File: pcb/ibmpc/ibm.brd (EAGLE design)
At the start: 124 x 56 mm, 32 parts, among them J2 ATX24RH

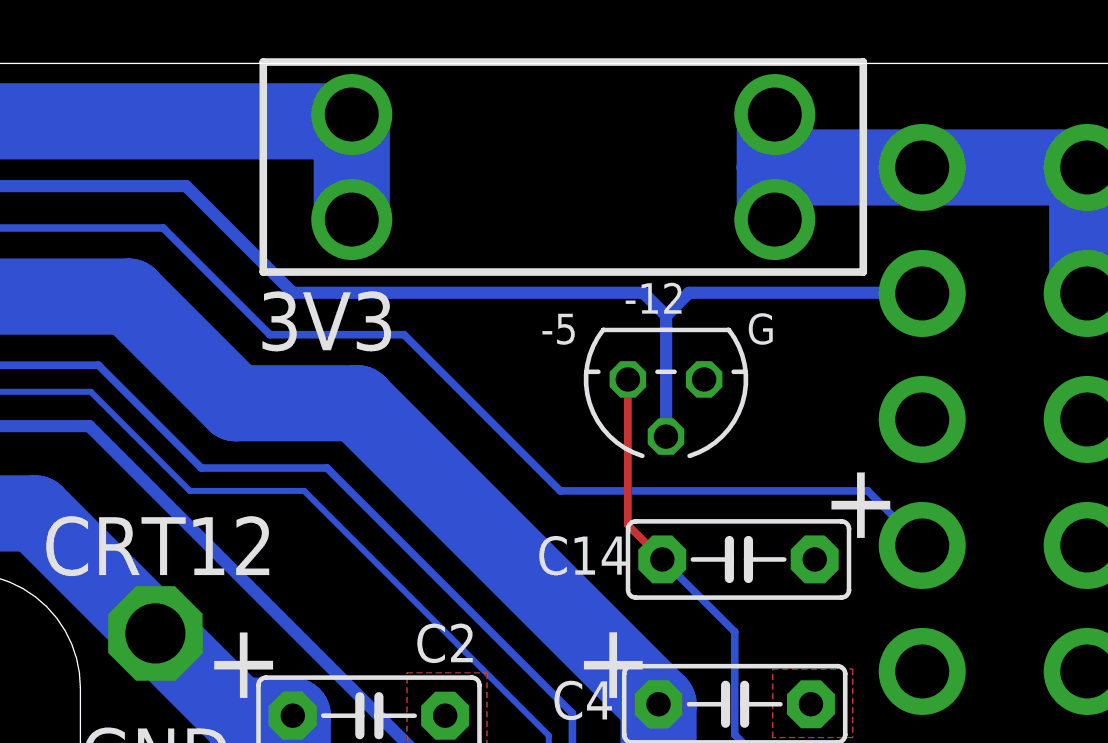
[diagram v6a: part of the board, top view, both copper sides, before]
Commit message: switched back to 7905
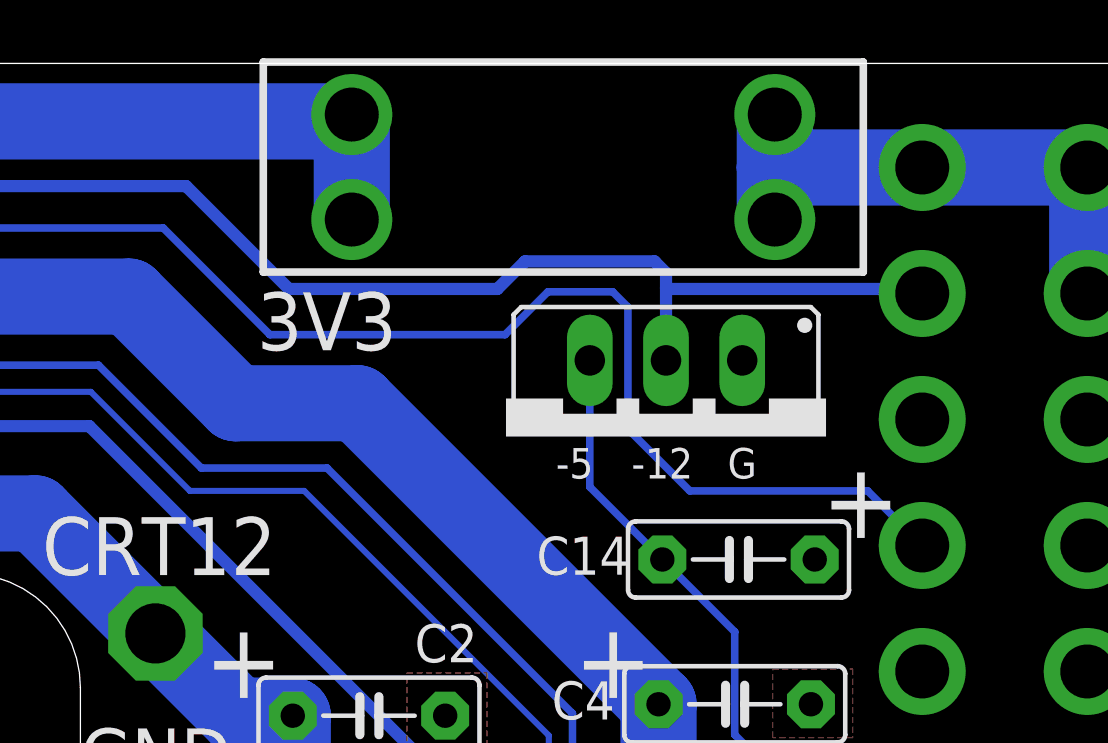
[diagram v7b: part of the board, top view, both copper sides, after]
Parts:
- removed IC2: (no value), linear:TO92
- added IC1: (no value), v-reg:79XXS
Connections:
- net GND: now also IC1.GND; no longer IC2.1
- net N$2: now also IC1.IN; no longer IC2.2
- net N$7: now also IC1.OUT; no longer IC2.3
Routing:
- net N$3: track 98.9 -> 102.5 mm
- net N$2: track 83.3 -> 82.1 mm
- net N$7: track 98.4 -> 99.6 mm
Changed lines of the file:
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@@
 <rectangle x1="67.823" y1="38.576" x2="72.014" y2="43.529" layer="41"/>
 <text x="15.6906" y="18.3234" size="2.54" layer="25" distance="35" align="center">picoRC.com</text>
-<text x="99.695" y="47.149" size="1.016" layer="25" rot="R180" align="center">G</text>
-<text x="96.139" y="48.165" size="1.016" layer="25" rot="R180" align="center">-12</text>
-<text x="92.964" y="47.149" size="1.016" layer="25" rot="R180" align="center">-5</text>
+<text x="99.06" y="42.672" size="1.016" layer="25" rot="R180" align="center">G</text>
+<text x="96.393" y="42.672" size="1.016" layer="25" rot="R180" align="center">-12</text>
+<text x="93.472" y="42.672" size="1.016" layer="25" rot="R180" align="center">-5</text>
 <text x="85.217" y="47.403" size="1.9304" layer="25" rot="R180" align="center">3V3</text>
 <text x="87.122" y="0.921" size="1.6764" layer="25" rot="R180" align="center">12V</text>
@@
 </element>
 <element name="U$7" library="apricot" package="M3_MOUNTING_HOLE_PACK" value="M3_MOUNTING_HOLE" x="80" y="22.75" smashed="yes"/>
-<element name="IC2" library="linear" library_urn="urn:adsk.eagle:library:262" package="TO92" package3d_urn="urn:adsk.eagle:package:16416/2" value="" x="96.52" y="45.466" smashed="yes" rot="R180">
-<attribute name="POPULARITY" value="0" x="96.52" y="45.466" size="1.778" layer="27" rot="R180" display="off"/>
-<attribute name="VALUE" x="93.599" y="46.736" size="1.27" layer="27" ratio="10" rot="R180"/>
+<element name="IC1" library="v-reg" library_urn="urn:adsk.eagle:library:409" package="79XXS" package3d_urn="urn:adsk.eagle:package:30343/1" value="" x="96.52" y="43.561" smashed="yes" rot="R180">
+<attribute name="POPULARITY" value="3" x="96.52" y="42.545" size="1.778" layer="27" rot="R180" display="off"/>
+<attribute name="VALUE" x="101.6" y="51.181" size="1.27" layer="27" ratio="10" rot="R180"/>
 </element>
 </elements>
@@
 <contactref element="U$7" pad="P$1"/>
 <contactref element="U$7" pad="P$2"/>
-<contactref element="IC2" pad="1"/>
 <wire x1="79.5" y1="30" x2="79.5" y2="23.25" width="2.54" layer="16"/>
 <wire x1="79.5" y1="23.25" x2="80" y2="22.75" width="2.54" layer="16"/>
+<contactref element="IC1" pad="GND"/>
 </signal>
 <signal name="+5V">
@@
 <contactref element="J2" pad="14"/>
 <contactref element="U$1" pad="P$12"/>
-<wire x1="105.061" y1="48.332" x2="105.038" y2="48.355" width="0.4064" layer="16"/>
-<wire x1="105.038" y1="48.355" x2="97.287" y2="48.355" width="0.4064" layer="16"/>
-<wire x1="97.287" y1="48.355" x2="96.525" y2="47.593" width="0.4064" layer="16"/>
-<wire x1="96.525" y1="47.593" x2="95.763" y2="48.355" width="0.4064" layer="16"/>
-<wire x1="95.763" y1="48.355" x2="84.079" y2="48.355" width="0.4064" layer="16"/>
+<wire x1="105.061" y1="48.332" x2="104.911" y2="48.482" width="0.4064" layer="16"/>
 <wire x1="40.55" y1="51.911" x2="36.359" y2="47.72" width="0.4064" layer="16"/>
 <wire x1="36.359" y1="47.72" x2="36.359" y2="46.577" width="0.4064" layer="16"/>
@@
 <wire x1="36.359" y1="46.577" x2="36.359" y2="41.059" width="0.4064" layer="1"/>
 <wire x1="36.359" y1="41.059" x2="36.3" y2="41" width="0.4064" layer="1"/>
-<wire x1="84.079" y1="48.355" x2="80.523" y2="51.911" width="0.4064" layer="16"/>
+<wire x1="83.952" y1="48.482" x2="80.523" y2="51.911" width="0.4064" layer="16"/>
 <wire x1="80.523" y1="51.911" x2="40.55" y2="51.911" width="0.4064" layer="16"/>
-<contactref element="IC2" pad="2"/>
-<wire x1="96.525" y1="43.566" x2="96.52" y2="43.561" width="0.4064" layer="16"/>
-<wire x1="96.525" y1="47.593" x2="96.525" y2="43.566" width="0.4064" layer="16"/>
+<contactref element="IC1" pad="IN"/>
+<wire x1="96.52" y1="49.022" x2="96.139" y2="49.403" width="0.4064" layer="16"/>
+<wire x1="96.139" y1="49.403" x2="91.821" y2="49.403" width="0.4064" layer="16"/>
+<wire x1="90.9" y1="48.482" x2="83.952" y2="48.482" width="0.4064" layer="16"/>
+<wire x1="96.52" y1="46.101" x2="96.52" y2="48.514" width="0.4064" layer="16"/>
+<wire x1="96.52" y1="48.514" x2="96.52" y2="49.022" width="0.4064" layer="16"/>
+<wire x1="91.821" y1="49.403" x2="90.9" y2="48.482" width="0.4064" layer="16"/>
+<wire x1="96.552" y1="48.482" x2="96.52" y2="48.514" width="0.4064" layer="16"/>
+<wire x1="104.911" y1="48.482" x2="96.552" y2="48.482" width="0.4064" layer="16"/>
 </signal>
 <signal name="N$3">
@@
 <wire x1="28.39" y1="39.783" x2="24.633" y2="39.783" width="0.2032" layer="1"/>
 <wire x1="29.596" y1="40.989" x2="28.39" y2="39.783" width="0.2032" layer="1"/>
-<wire x1="87.789" y1="46.958" x2="83.317" y2="46.958" width="0.254" layer="16"/>
-<wire x1="103.242" y1="41.751" x2="92.996" y2="41.751" width="0.254" layer="16"/>
-<wire x1="92.996" y1="41.751" x2="87.789" y2="46.958" width="0.254" layer="16"/>
+<wire x1="103.242" y1="41.751" x2="97.314" y2="41.751" width="0.254" layer="16"/>
+<wire x1="95.25" y1="47.879" x2="94.742" y2="48.387" width="0.254" layer="16"/>
+<wire x1="94.742" y1="48.387" x2="92.583" y2="48.387" width="0.254" layer="16"/>
+<wire x1="97.314" y1="41.751" x2="95.25" y2="43.815" width="0.254" layer="16"/>
+<wire x1="95.25" y1="43.815" x2="95.25" y2="47.879" width="0.254" layer="16"/>
+<wire x1="92.583" y1="48.387" x2="91.154" y2="46.958" width="0.254" layer="16"/>
+<wire x1="91.154" y1="46.958" x2="83.317" y2="46.958" width="0.254" layer="16"/>
 </signal>
 <signal name="N$4">
@@
 <wire x1="77.602" y1="45.942" x2="81.031" y2="42.513" width="0.254" layer="16"/>
 <wire x1="81.031" y1="42.513" x2="85.222" y2="42.513" width="0.254" layer="16"/>
-<contactref element="IC2" pad="3"/>
-<wire x1="95.25" y1="45.466" x2="95.25" y2="40.613" width="0.254" layer="1"/>
-<wire x1="95.25" y1="40.613" x2="96.398" y2="39.465" width="0.254" layer="1"/>
+<contactref element="IC1" pad="OUT"/>
+<wire x1="93.98" y1="46.101" x2="93.98" y2="41.883" width="0.254" layer="16"/>
+<wire x1="93.98" y1="41.883" x2="96.398" y2="39.465" width="0.254" layer="16"/>
 </signal>
 <signal name="N$9">

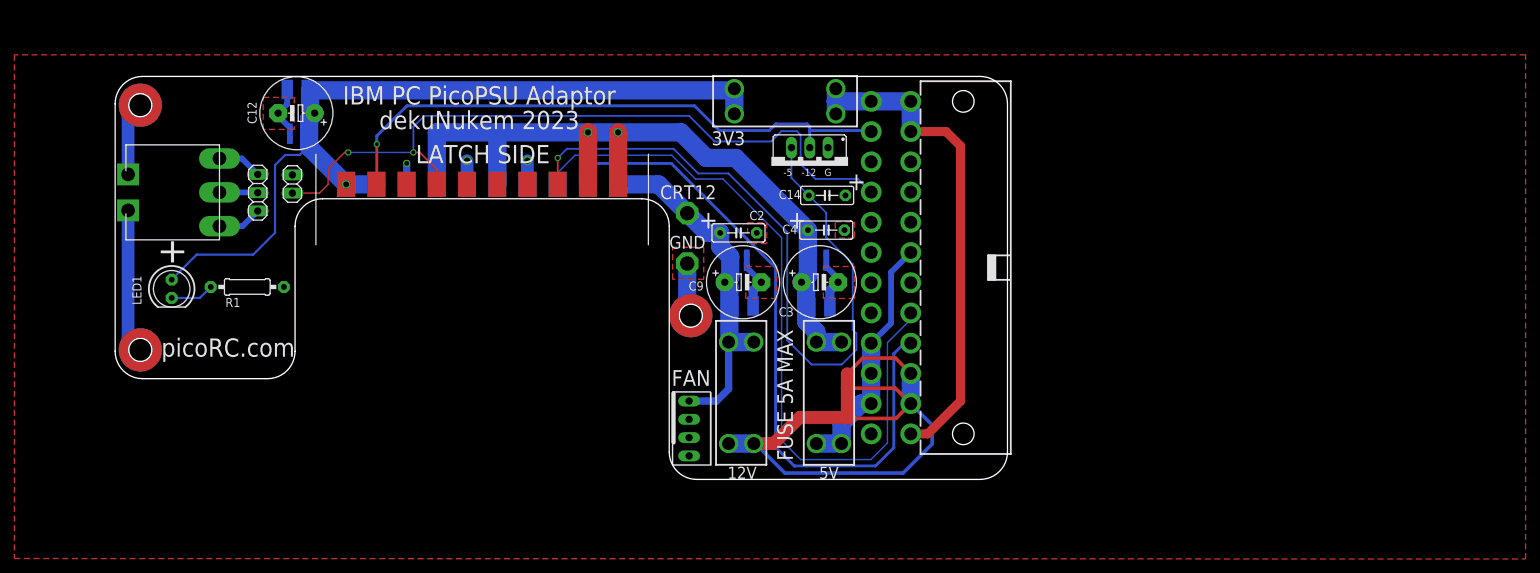
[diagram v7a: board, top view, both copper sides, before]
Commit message: added ISA legs
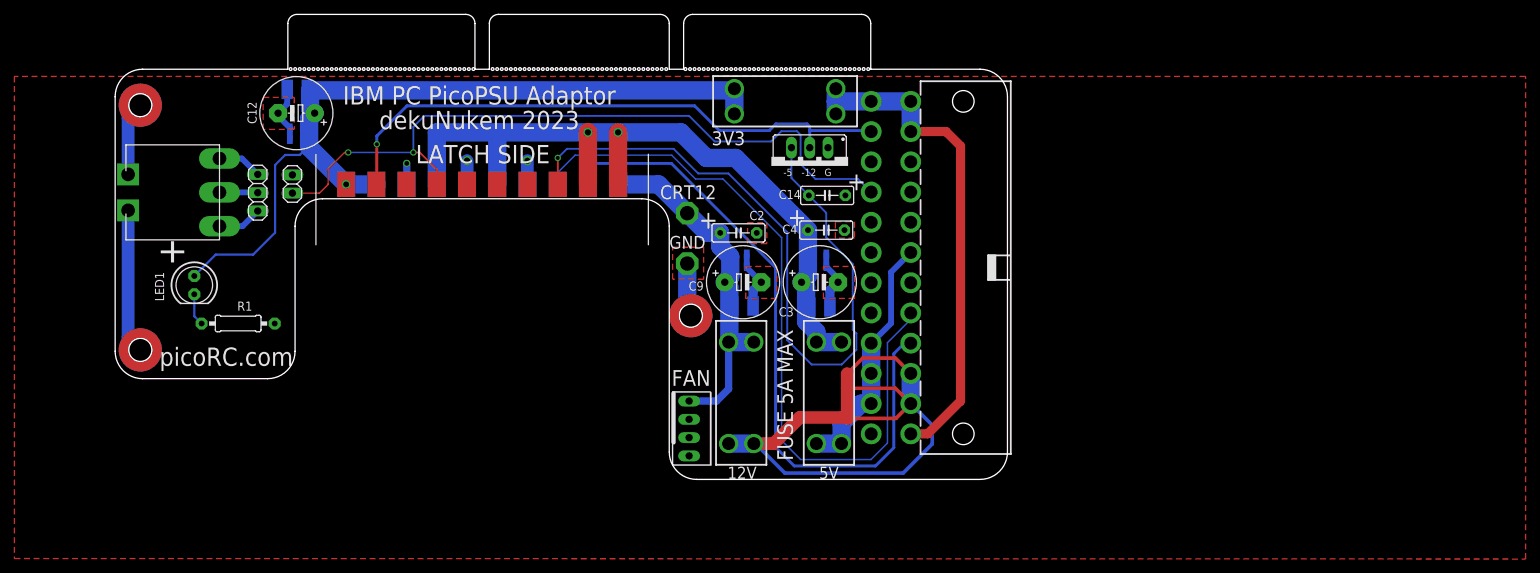
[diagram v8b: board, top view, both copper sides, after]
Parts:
- moved R1 5.24 mm to (17.1, 21.7)
- moved LED1 3.18 mm to (11.0, 27.0)
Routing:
- net +3V3: track 127.9 -> 124.5 mm
- net N$12: track 6.06 -> 4.49 mm
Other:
- board size 124 x 56 mm -> 124 x 64.6 mm
